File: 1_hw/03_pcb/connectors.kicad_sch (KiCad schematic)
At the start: 15 parts, among them J1 TYPE-C-31-M-12, J2 SMA, J3 SMA, J4 BNC, J5 PH-00244

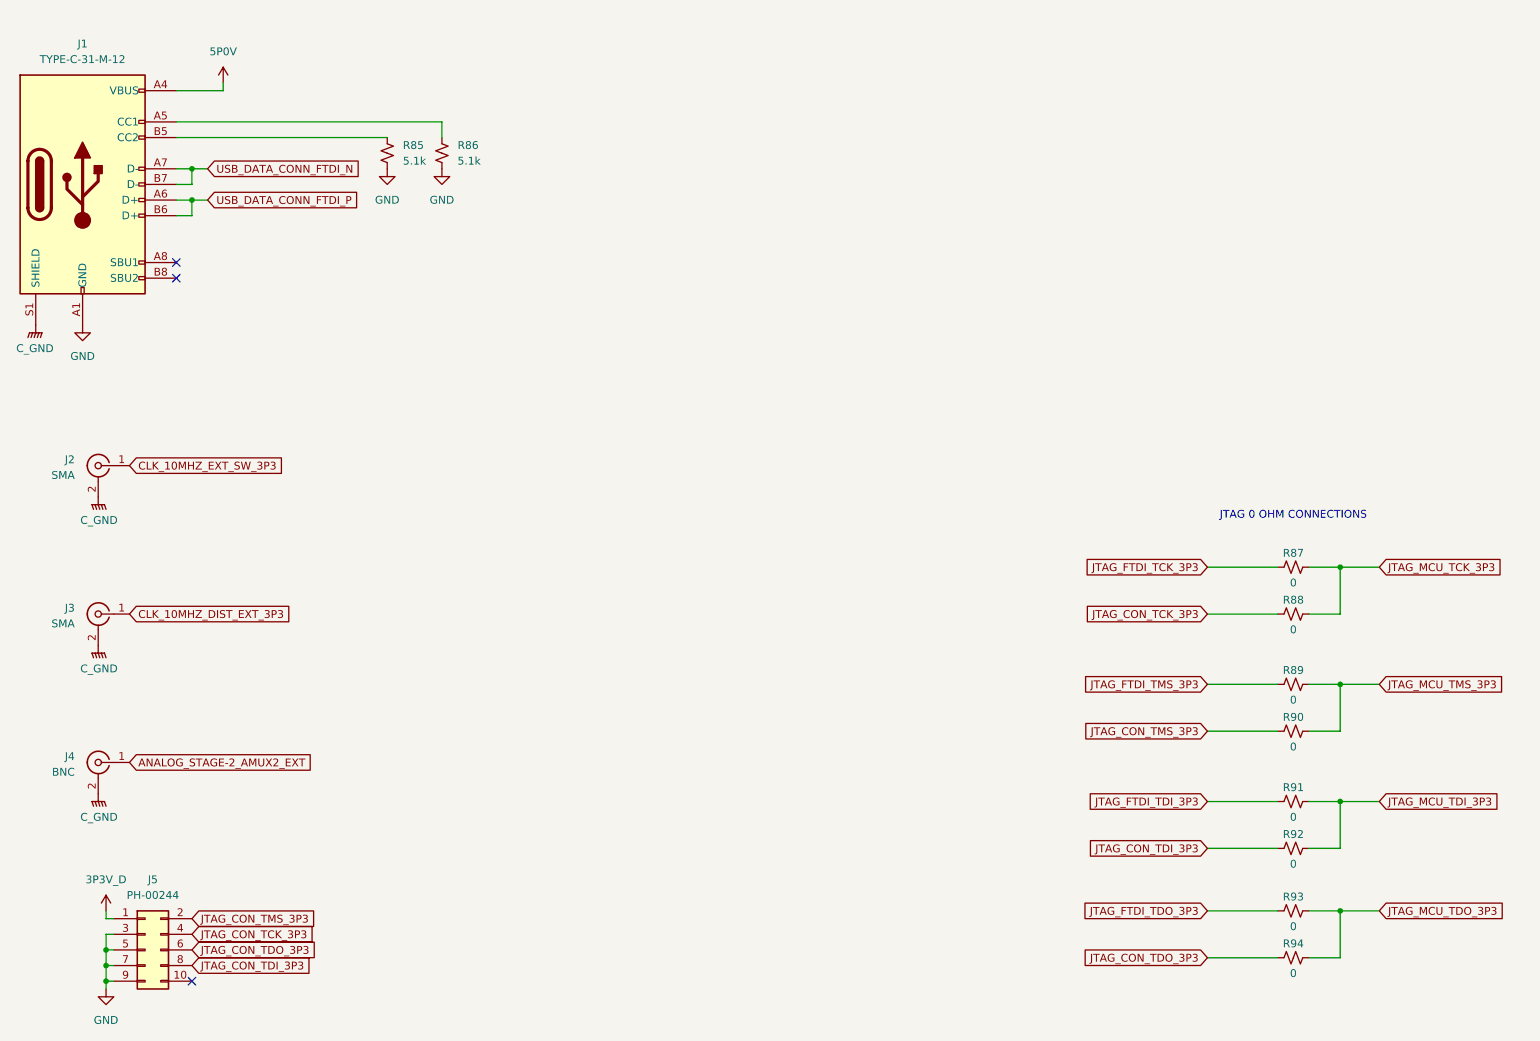
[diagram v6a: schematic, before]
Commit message: MINOR: Verified Footprints to Datasheets. Added Pull Ups on FPGA DONE/Config/SPI Chip Select Pins.
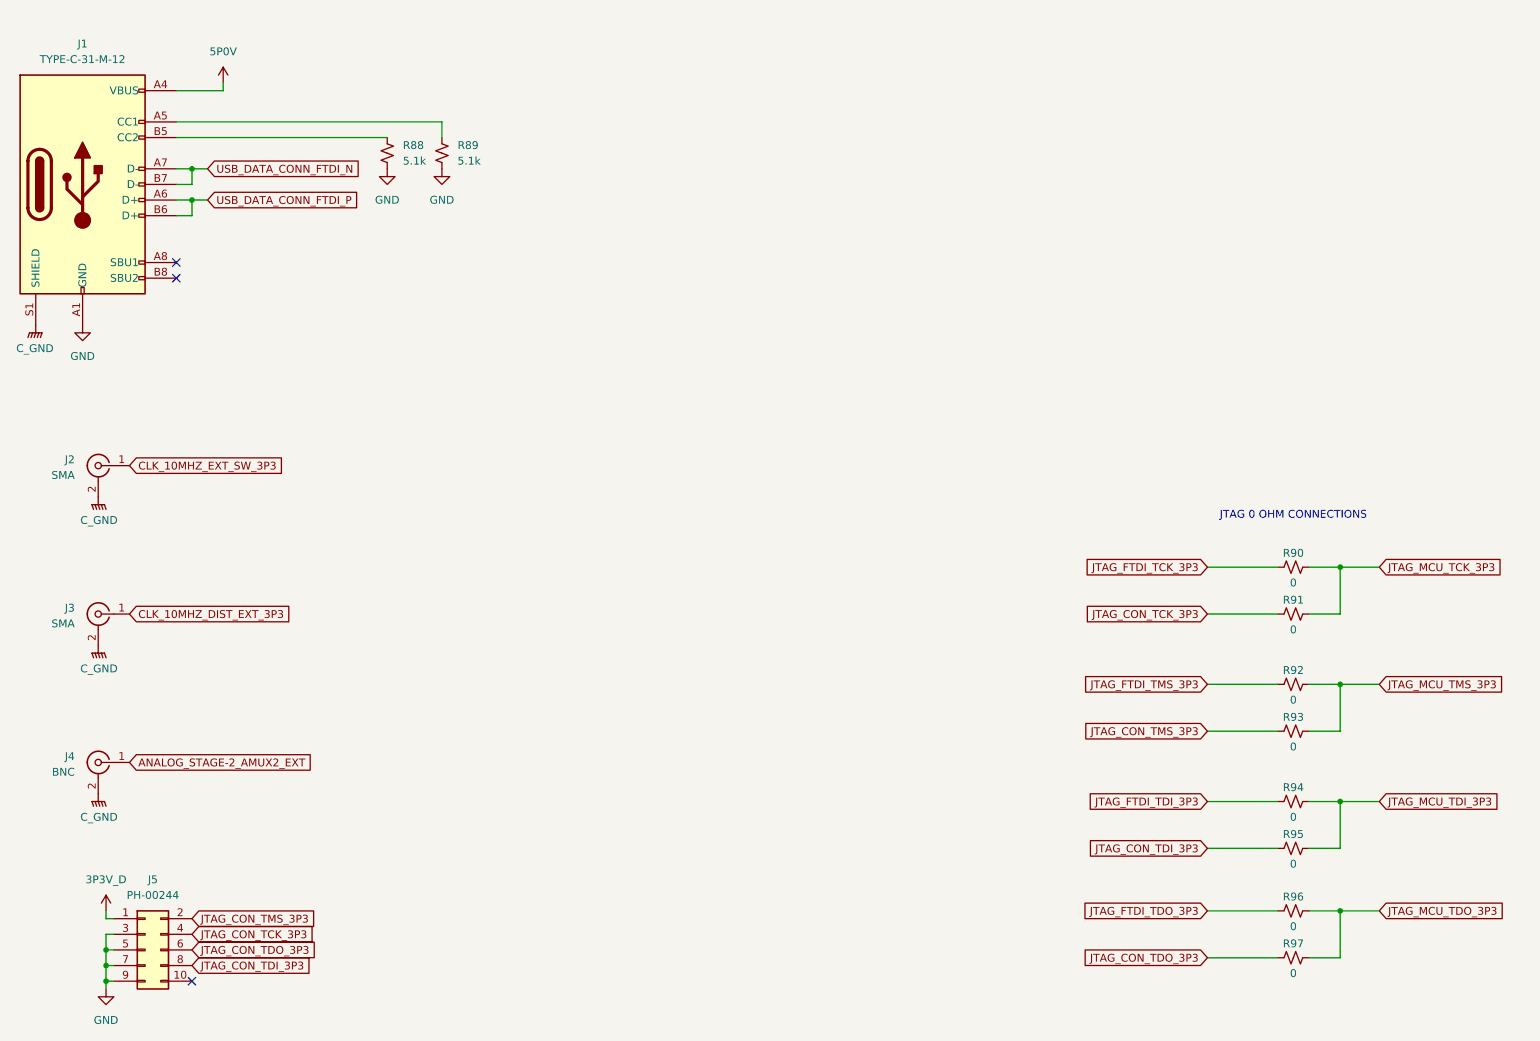
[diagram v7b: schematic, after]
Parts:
- renumbered R85 to R88, R86 to R89, R87 to R90, R88 to R91, R89 to R92, R90 to R93, R91 to R94, R92 to R95, R93 to R96, R94 to R97
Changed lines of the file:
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@@
 		(on_board yes)
 		(dnp no)
-		(property "Reference" "R94"
+		(property "Reference" "R97"
 			(at 229.87 165.354 90)
 			(effects
@@
 			(project "arb"
 				(path "/866ef9be-3b01-4288-a6e0-a2357aa17e50/eb105004-087f-4ea7-8291-809b214299af"
-					(reference "R94")
+					(reference "R97")
 					(unit 1)
 				)
@@
 		(dnp no)
 		(fields_autoplaced yes)
-		(property "Reference" "#PWR0281"
+		(property "Reference" "#PWR0284"
 			(at 35.56 121.92 0)
 			(effects
@@
 			(project "arb"
 				(path "/866ef9be-3b01-4288-a6e0-a2357aa17e50/eb105004-087f-4ea7-8291-809b214299af"
-					(reference "#PWR0281")
+					(reference "#PWR0284")
 					(unit 1)
 				)
@@
 		(dnp no)
 		(fields_autoplaced yes)
-		(property "Reference" "#PWR0283"
+		(property "Reference" "#PWR0286"
 			(at 36.83 163.83 0)
 			(effects
@@
 			(project "arb"
 				(path "/866ef9be-3b01-4288-a6e0-a2357aa17e50/eb105004-087f-4ea7-8291-809b214299af"
-					(reference "#PWR0283")
+					(reference "#PWR0286")
 					(unit 1)
 				)
@@
 		(on_board yes)
 		(dnp no)
-		(property "Reference" "R89"
+		(property "Reference" "R92"
 			(at 229.87 120.904 90)
 			(effects
@@
 			(project "arb"
 				(path "/866ef9be-3b01-4288-a6e0-a2357aa17e50/eb105004-087f-4ea7-8291-809b214299af"
-					(reference "R89")
+					(reference "R92")
 					(unit 1)
 				)
@@
 		(dnp no)
 		(fields_autoplaced yes)
-		(property "Reference" "R86"
+		(property "Reference" "R89"
 			(at 93.98 35.5599 0)
 			(effects
@@
 			(project "arb"
 				(path "/866ef9be-3b01-4288-a6e0-a2357aa17e50/eb105004-087f-4ea7-8291-809b214299af"
-					(reference "R86")
+					(reference "R89")
 					(unit 1)
 				)
@@
 		(dnp no)
 		(fields_autoplaced yes)
-		(property "Reference" "#PWR0286"
+		(property "Reference" "#PWR0289"
 			(at 82.55 45.72 0)
 			(effects
@@
 			(project "arb"
 				(path "/866ef9be-3b01-4288-a6e0-a2357aa17e50/eb105004-087f-4ea7-8291-809b214299af"
-					(reference "#PWR0286")
+					(reference "#PWR0289")
 					(unit 1)
 				)
@@
 		(dnp no)
 		(fields_autoplaced yes)
-		(property "Reference" "#PWR0282"
+		(property "Reference" "#PWR0285"
 			(at 35.56 146.05 0)
 			(effects
@@
 			(project "arb"
 				(path "/866ef9be-3b01-4288-a6e0-a2357aa17e50/eb105004-087f-4ea7-8291-809b214299af"
-					(reference "#PWR0282")
+					(reference "#PWR0285")
 					(unit 1)
 				)
@@
 		(dnp no)
 		(fields_autoplaced yes)
-		(property "Reference" "#PWR0284"
+		(property "Reference" "#PWR0287"
 			(at 36.83 179.07 0)
 			(effects
@@
 			(project "arb"
 				(path "/866ef9be-3b01-4288-a6e0-a2357aa17e50/eb105004-087f-4ea7-8291-809b214299af"
-					(reference "#PWR0284")
+					(reference "#PWR0287")
 					(unit 1)
 				)
@@
 		(dnp no)
 		(fields_autoplaced yes)
-		(property "Reference" "#PWR0287"
+		(property "Reference" "#PWR0290"
 			(at 91.44 45.72 0)
 			(effects
@@
 			(project "arb"
 				(path "/866ef9be-3b01-4288-a6e0-a2357aa17e50/eb105004-087f-4ea7-8291-809b214299af"
-					(reference "#PWR0287")
+					(reference "#PWR0290")
 					(unit 1)
 				)
@@
 		(dnp no)
 		(fields_autoplaced yes)
-		(property "Reference" "#PWR0278"
+		(property "Reference" "#PWR0281"
 			(at 25.4 69.85 0)
 			(effects
@@
 			(project "arb"
 				(path "/866ef9be-3b01-4288-a6e0-a2357aa17e50/eb105004-087f-4ea7-8291-809b214299af"
-					(reference "#PWR0278")
+					(reference "#PWR0281")
 					(unit 1)
 				)
@@
 		(on_board yes)
 		(dnp no)
-		(property "Reference" "R88"
+		(property "Reference" "R91"
 			(at 229.87 109.474 90)
 			(effects
@@
 			(project "arb"
 				(path "/866ef9be-3b01-4288-a6e0-a2357aa17e50/eb105004-087f-4ea7-8291-809b214299af"
-					(reference "R88")
+					(reference "R91")
 					(unit 1)
 				)
@@
 		(on_board yes)
 		(dnp no)
-		(property "Reference" "R91"
+		(property "Reference" "R94"
 			(at 229.87 139.954 90)
 			(effects
@@
 			(project "arb"
 				(path "/866ef9be-3b01-4288-a6e0-a2357aa17e50/eb105004-087f-4ea7-8291-809b214299af"
-					(reference "R91")
+					(reference "R94")
 					(unit 1)
 				)
@@
 		(dnp no)
 		(fields_autoplaced yes)
-		(property "Reference" "#PWR0279"
+		(property "Reference" "#PWR0282"
 			(at 33.02 71.12 0)
 			(effects
@@
 			(project "arb"
 				(path "/866ef9be-3b01-4288-a6e0-a2357aa17e50/eb105004-087f-4ea7-8291-809b214299af"
-					(reference "#PWR0279")
+					(reference "#PWR0282")
 					(unit 1)
 				)
@@
 		(on_board yes)
 		(dnp no)
-		(property "Reference" "R92"
+		(property "Reference" "R95"
 			(at 229.87 147.574 90)
 			(effects
@@
 			(project "arb"
 				(path "/866ef9be-3b01-4288-a6e0-a2357aa17e50/eb105004-087f-4ea7-8291-809b214299af"
-					(reference "R92")
+					(reference "R95")
 					(unit 1)
 				)
@@
 		(on_board yes)
 		(dnp no)
-		(property "Reference" "R93"
+		(property "Reference" "R96"
 			(at 229.87 157.734 90)
 			(effects
@@
 			(project "arb"
 				(path "/866ef9be-3b01-4288-a6e0-a2357aa17e50/eb105004-087f-4ea7-8291-809b214299af"
-					(reference "R93")
+					(reference "R96")
 					(unit 1)
 				)
@@
 		(on_board yes)
 		(dnp no)
-		(property "Reference" "R87"
+		(property "Reference" "R90"
 			(at 229.87 101.854 90)
 			(effects
@@
 			(project "arb"
 				(path "/866ef9be-3b01-4288-a6e0-a2357aa17e50/eb105004-087f-4ea7-8291-809b214299af"
-					(reference "R87")
+					(reference "R90")
 					(unit 1)
 				)
@@
 		(dnp no)
 		(fields_autoplaced yes)
-		(property "Reference" "#PWR0285"
+		(property "Reference" "#PWR0288"
 			(at 55.88 29.21 0)
 			(effects
@@
 			(project "arb"
 				(path "/866ef9be-3b01-4288-a6e0-a2357aa17e50/eb105004-087f-4ea7-8291-809b214299af"
-					(reference "#PWR0285")
+					(reference "#PWR0288")
 					(unit 1)
 				)
@@
 		(dnp no)
 		(fields_autoplaced yes)
-		(property "Reference" "R85"
+		(property "Reference" "R88"
 			(at 85.09 35.5599 0)
 			(effects
@@
 			(project "arb"
 				(path "/866ef9be-3b01-4288-a6e0-a2357aa17e50/eb105004-087f-4ea7-8291-809b214299af"
-					(reference "R85")
+					(reference "R88")
 					(unit 1)
 				)
@@
 		(dnp no)
 		(fields_autoplaced yes)
-		(property "Reference" "#PWR0280"
+		(property "Reference" "#PWR0283"
 			(at 35.56 97.79 0)
 			(effects
@@
 			(project "arb"
 				(path "/866ef9be-3b01-4288-a6e0-a2357aa17e50/eb105004-087f-4ea7-8291-809b214299af"
-					(reference "#PWR0280")
+					(reference "#PWR0283")
 					(unit 1)
 				)
@@
 		(on_board yes)
 		(dnp no)
-		(property "Reference" "R90"
+		(property "Reference" "R93"
 			(at 229.87 128.524 90)
 			(effects
@@
 			(project "arb"
 				(path "/866ef9be-3b01-4288-a6e0-a2357aa17e50/eb105004-087f-4ea7-8291-809b214299af"
-					(reference "R90")
-					(unit 1)
-				)
+					(reference "R93")
+					(unit 1)
+				)

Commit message: MINOR: Added Board Rules & Constraints.
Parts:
- added H1, H2, H3, H4: MOUNTING HOLE, MountingHole_3.2mm_M3_Pad, symbol Mechanical:MountingHole_Pad
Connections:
- net C_GND: now also H1.1, H2.1, H3.1, H4.1
